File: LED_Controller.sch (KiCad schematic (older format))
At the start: 38 parts, among them CON1 CONNECTOR, CON2 CONNECTOR, CON3 CONNECTOR, CON4 CONNECTOR, CON5 PWR_CON, CON6 AVR-ISP-10, IC1 ATMEGA328P-P, Q1 STS8DN3LLH5, Q2 STS8DN3LLH5, Q3 STS8DN3LLH5

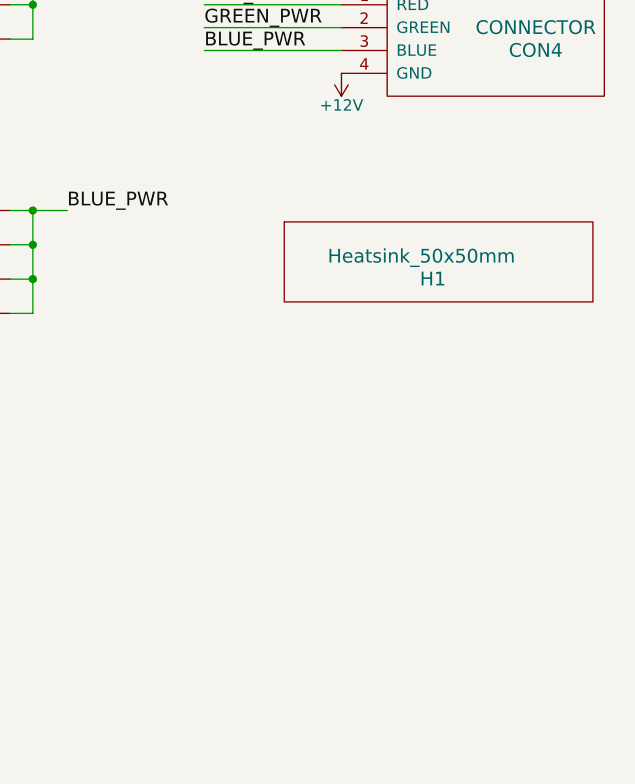
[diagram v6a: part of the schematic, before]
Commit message: More output pins for LED strips, mounting holes added
Updated size of LED output holes for LED strips

Added more output footprints for strips

Added mounting holes to corners of board; are probably incorrect size,
modify later

Exported updated gerbers
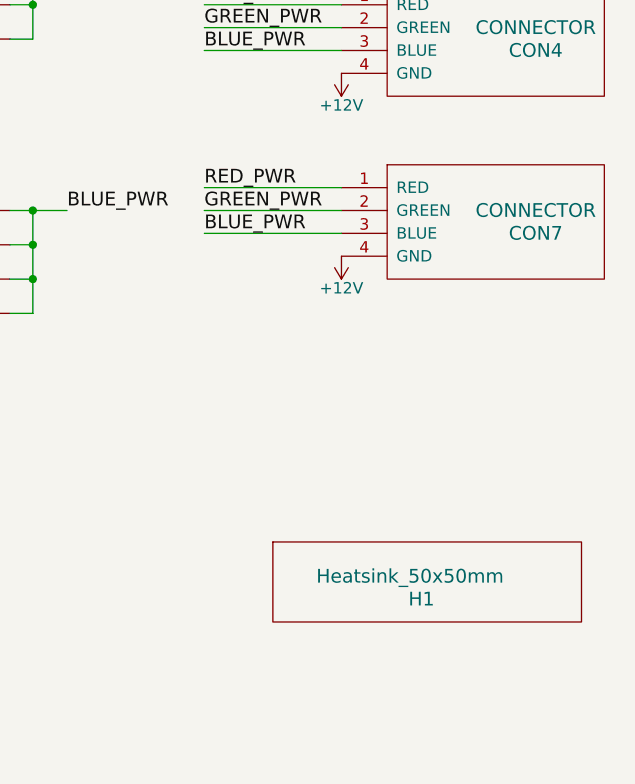
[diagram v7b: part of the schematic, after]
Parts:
- added CON7: CONNECTOR, LED_controller_footprints:OUTPUT_HOLES, symbol CONNECTOR
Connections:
- net +12V: now also CON7.4 (GND)
- net BLUE_PWR: now also CON7.3 (BLUE)
- net GREEN_PWR: now also CON7.2 (GREEN)
- net RED_PWR: now also CON7.1 (RED)
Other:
- moved on the sheet: H1
